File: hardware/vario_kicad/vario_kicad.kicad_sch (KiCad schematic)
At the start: 32 parts, among them P1 USB_C_Plug_USB2.0, U2 BME280, U3 W25Q128JVS, U4 STM32L072CBTx

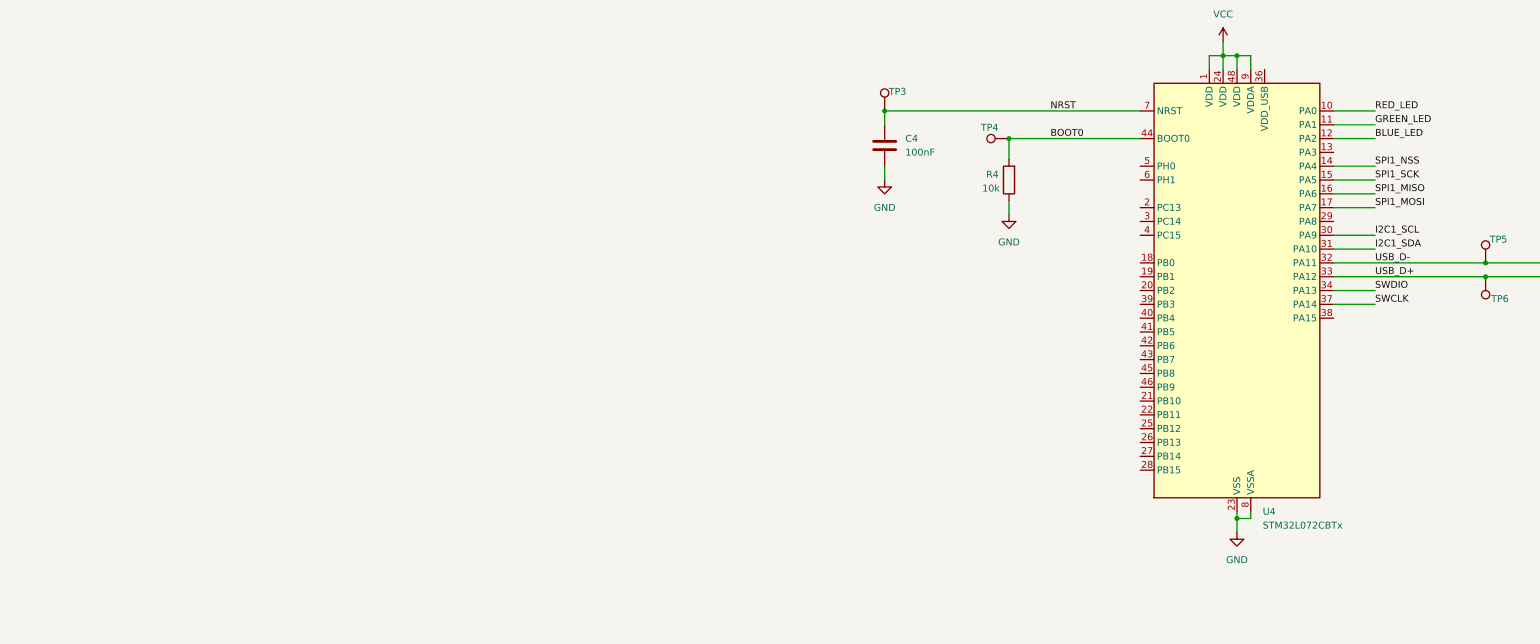
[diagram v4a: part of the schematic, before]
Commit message: add NS4150B symbol
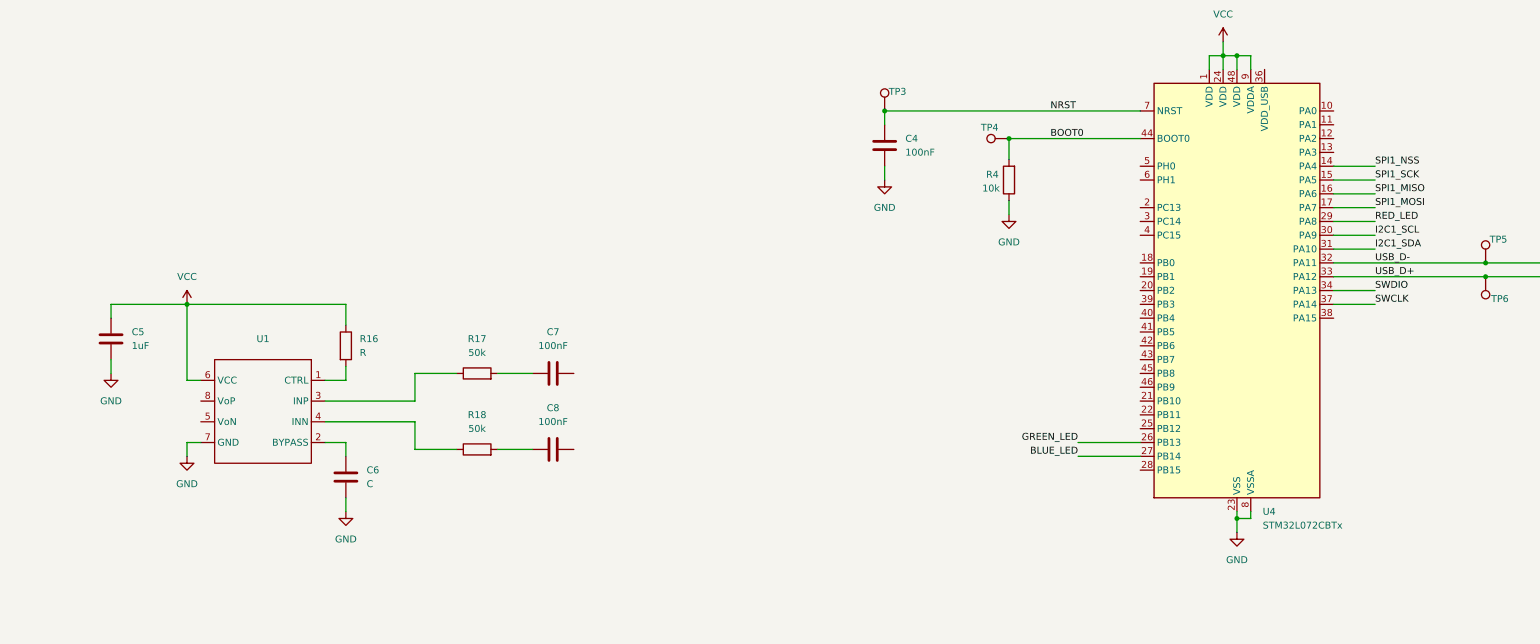
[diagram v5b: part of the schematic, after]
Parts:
- added C5: 1uF, symbol Device:C
- added C6: C, symbol Device:C
- added C7, C8: 100nF, symbol Device:C
- added R16: R, symbol Device:R
- added R17, R18: 50k, symbol Device:R
- added U1: ~, Package_SO:MSOP-8-1EP_3x3mm_P0.65mm_EP1.73x1.85mm, symbol New_Library:NS4150B
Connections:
- net BLUE_LED: now also U4.27 (PB14); no longer U4.12 (PA2)
- net GND: now also C5.2, C6.2, U1.7 (GND)
- net GREEN_LED: now also U4.26 (PB13); no longer U4.11 (PA1)
- net RED_LED: now also U4.29 (PA8); no longer U4.10 (PA0)
- net VCC: now also C5.1, R16.1, U1.6 (VCC)
- new net: R16.2, U1.1 (CTRL)
- new net: C6.1, U1.2 (BYPASS)
- new net: R17.1, U1.3 (INP)
- new net: R18.1, U1.4 (INN)
- new net: C7.1, R17.2
- new net: C8.1, R18.2

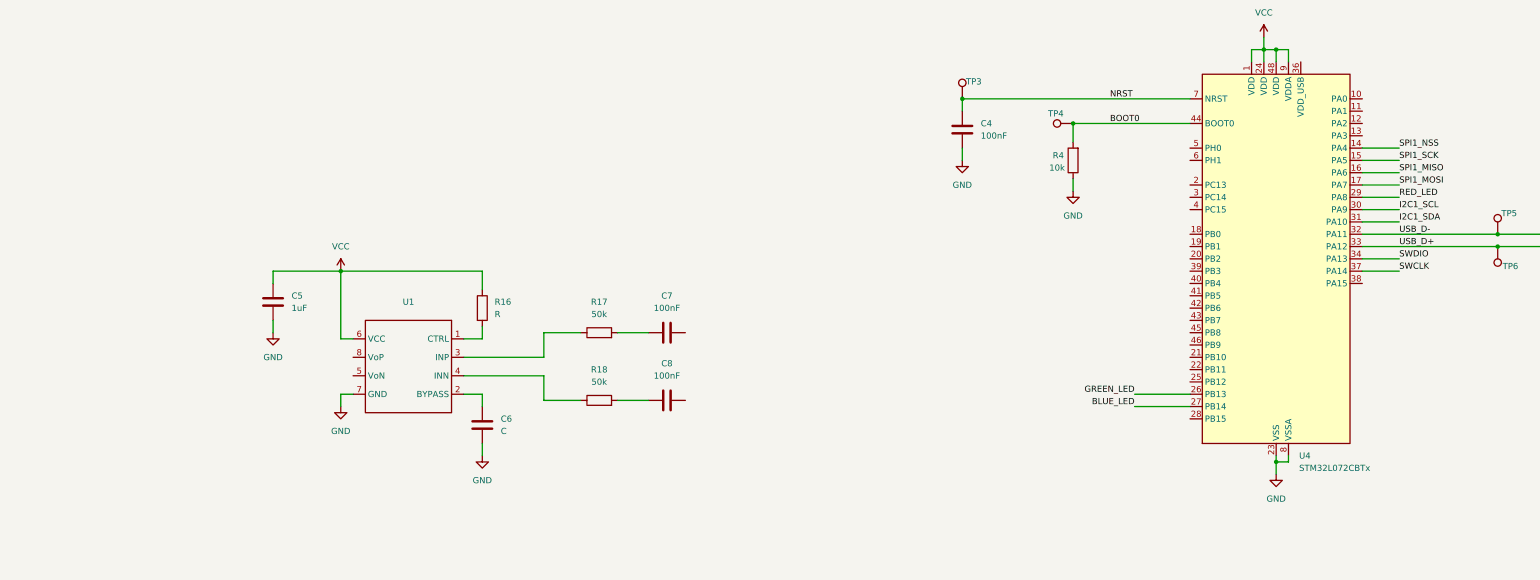
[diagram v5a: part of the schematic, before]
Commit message: update schematic, add stm32mx file
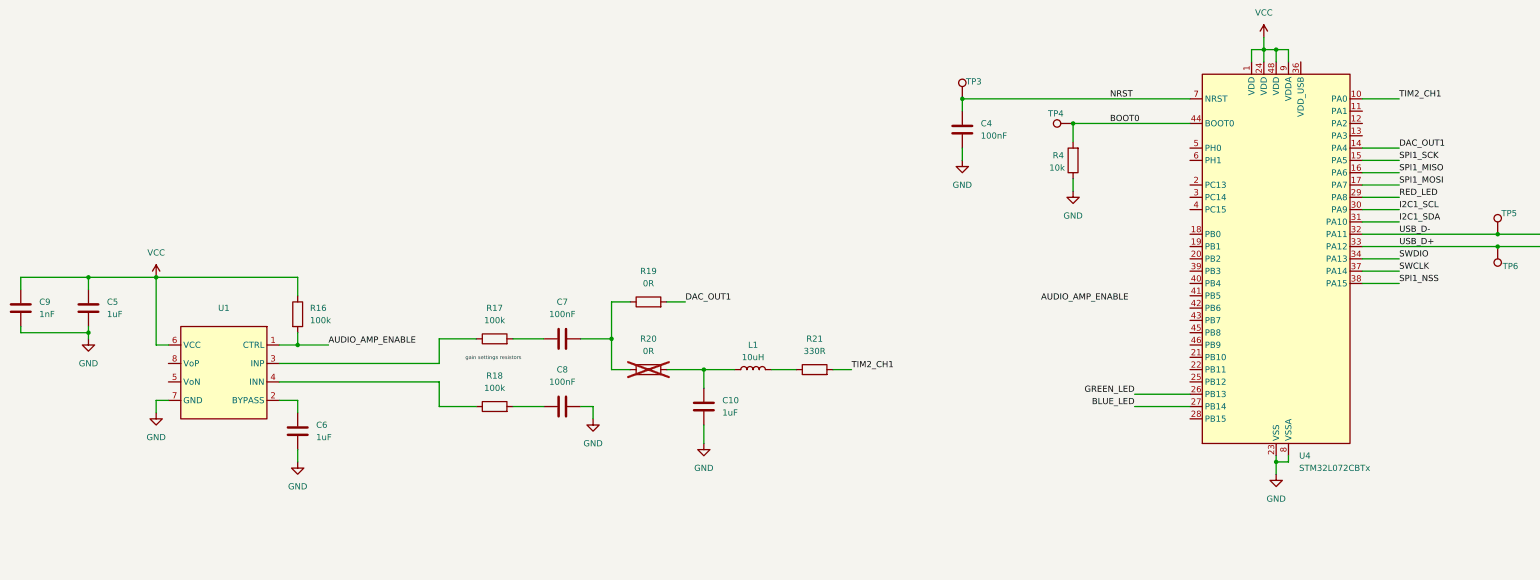
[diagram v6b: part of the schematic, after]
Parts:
- added C10: 1uF, symbol Device:C
- added C9: 1nF, symbol Device:C
- added L1: 10uH, symbol Device:L
- added R19, R20: 0R, symbol Device:R
- added R21: 330R, symbol Device:R
- C6: value C -> 1uF
- R16: value R -> 100k
- R17, R18: value 50k -> 100k
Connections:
- net GND: now also C8.2, C10.2, C9.2
- net SPI1_NSS: now also U4.38 (PA15); no longer U4.14 (PA4)
- net VCC: now also C9.1
- net TIM2_CH1: now reaches U4.10 (PA0)
- net TIM2_CH1: now also R21.2
- net AUDIO_AMP_ENABLE: now reaches R16.2, U1.1 (CTRL)
- net at C7.2: now also R19.1, R20.1
- new net: L1.2, R21.1
- new net: C10.1, L1.1, R20.2
- new net DAC_OUT1: R19.2, U4.14 (PA4)
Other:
- note added: "gain settings resistors"
- moved on the sheet: C5, C6, C7, C8, R16, R17, R18

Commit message: update
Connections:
- net AUDIO_AMP_ENABLE: now also U4.11 (PA1)
- net MEM_CS_ALT: now also U4.12 (PA2)
- net MEM_HOLD: now also U4.18 (PB0)
- net MEM_WP: now also U4.19 (PB1)
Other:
- moved on the sheet: C10, C5, C6, C7, C8, C9, L1, R16, R17, R18, R19, R20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

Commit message: add power supply
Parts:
- added BT1: Battery_Cell, symbol Device:Battery_Cell
- added C11, C12, C13: 1uF, symbol Device:C
- added D4: LED, symbol Device:LED
- added R22: 10mR, symbol Device:R
- added R23: 330R, symbol Device:R
- added R24: 10k, symbol Device:R
- added TP7, TP8: TestPoint, symbol Connector:TestPoint
- added U5: ~, Package_TO_SOT_SMD:SOT-23-5, symbol New_Library:TP4054
- added U6: ~, Package_TO_SOT_SMD:SOT-23, symbol New_Library:____XC6206P332MR-G
- R12, R13, R14: value 330R -> 1k
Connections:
- net GND: now also C11.2, C12.2, C13.2, R22.2, R24.2, U5.2 (GND), U6.1 (VSS)
- net VCC: now also C13.1, TP8.1, U6.2 (VOUT); no longer C5.1, C9.1, R16.1, U1.6 (VCC)
- net BLUE_LED renamed LED3
- net GREEN_LED renamed LED2
- net RED_LED renamed LED1
- net VBUS renamed V_USB
- net V_USB: now also C11.1, D4.2 (A), U5.4 (VCC)
- new net: D4.1 (K), R23.1
- new net: R23.2, U5.1 (~{CHRG})
- new net: R24.1, U5.5 (PROG)
- new net: BT1.2 (-), R22.1
- new net VBATT: BT1.1 (+), C12.1, C5.1, C9.1, R16.1, TP7.1, U1.6 (VCC), U5.3 (BAT), U6.2 (VOUT)
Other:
- note added: "TODO add a current sense amplifier"
